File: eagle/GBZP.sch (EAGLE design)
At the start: 35 parts, among them CN1 USB-SMD-NS, J3 battery, X3 16MHz

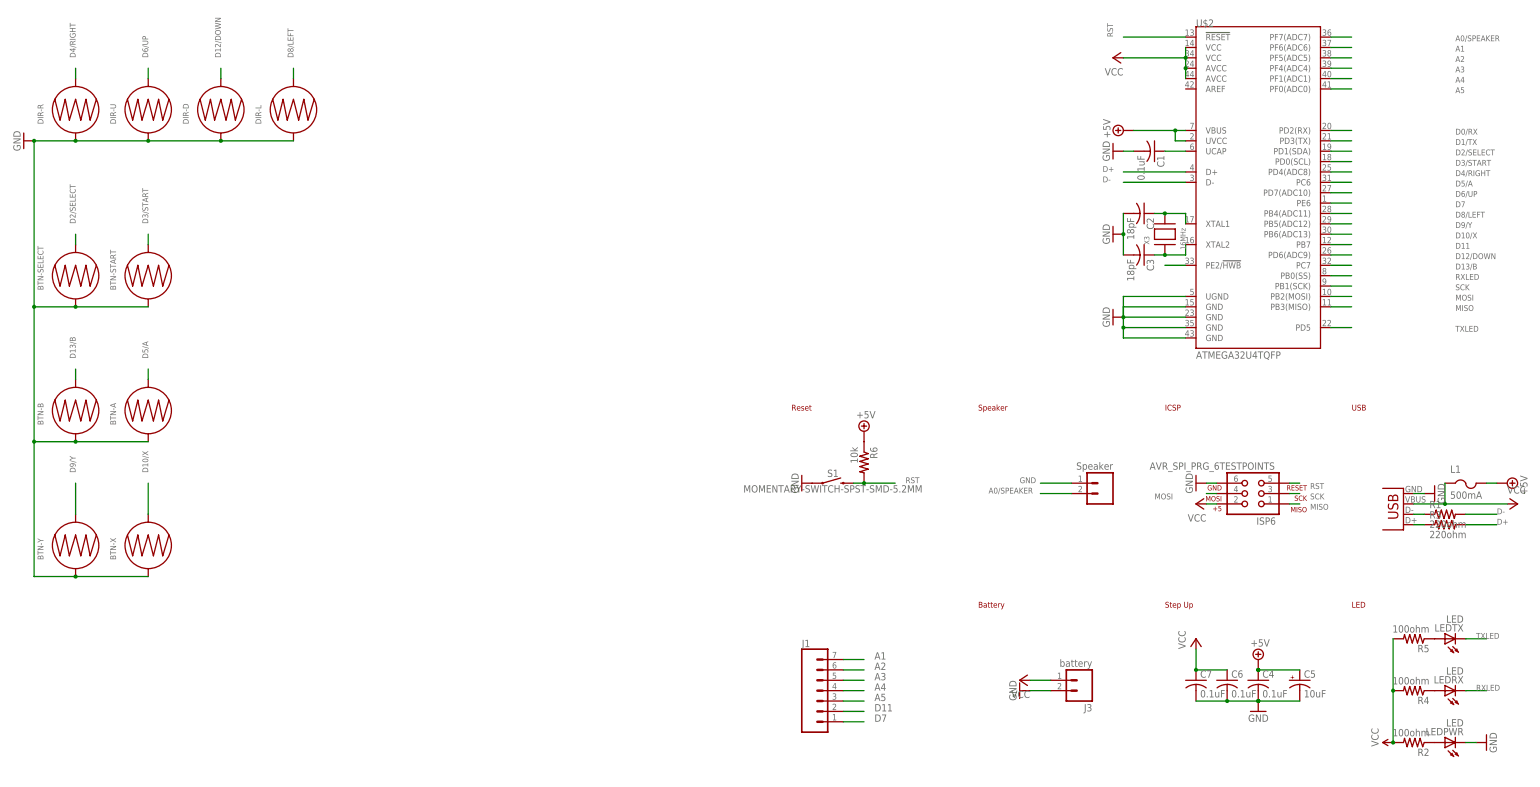
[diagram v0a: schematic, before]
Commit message: new pinout to match GBZ project
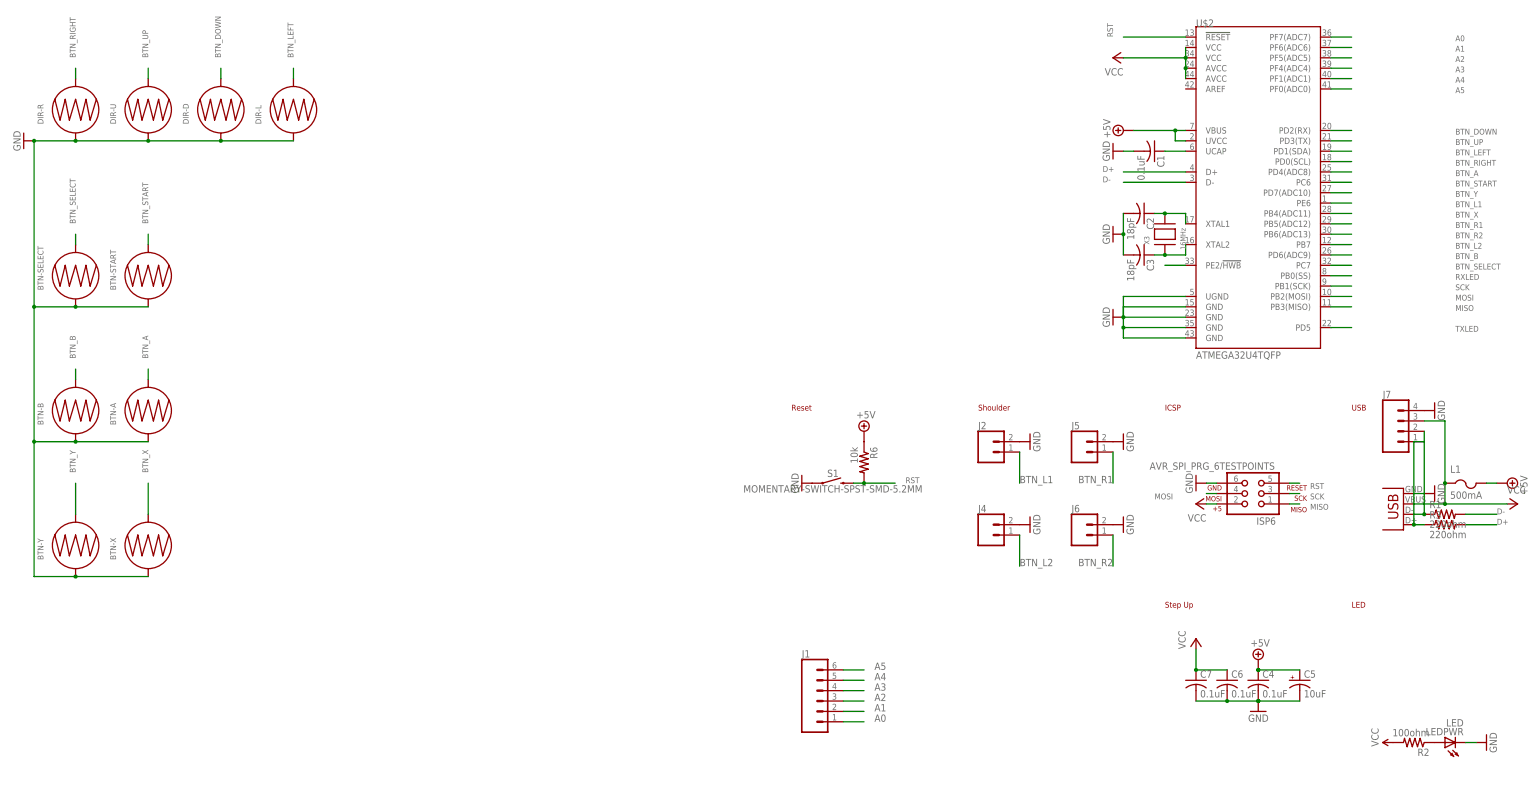
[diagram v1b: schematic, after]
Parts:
- removed J3: battery, SparkFun-Connectors:M021X02_NO_SILK
- removed JP2: Speaker, SparkFun-Connectors:M021X02_NO_SILK
- removed LEDRX, LEDTX: LED, adafruit:LEDCHIPLED_0805
- removed R4, R5: 100ohm, adafruit:R-US_R0805
- added J2, J4, J5, J6: (no value), SparkFun-Connectors:CONN_021X02_NO_SILK
- added J7: (no value), SparkFun-Connectors:CONN_041X04_NO_SILK
- J1: device SparkFun-Connectors:CONN_07NO_SILK -> SparkFun-Connectors:CONN_06NO_SILK_FEMALE_PTH
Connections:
- removed net A0/SPEAKER: JP2.2, U$2.PF7(ADC7)
- removed net D0/RX: U$2.PD2(RX)
- removed net D1/TX: U$2.PD3(TX)
- removed net D10/X: BTN-X.2, U$2.PB6(ADC13)
- removed net D11: J1.2, U$2.PB7
- removed net D12/DOWN: DIR-D.2, U$2.PD6(ADC9)
- removed net D13/B: BTN-B.2, U$2.PC7
- removed net D2/SELECT: BTN-SELECT.2, U$2.PD1(SDA)
- removed net D3/START: BTN-START.2, U$2.PD0(SCL)
- removed net D4/RIGHT: DIR-R.2, U$2.PD4(ADC8)
- removed net D5/A: BTN-A.2, U$2.PC6
- removed net D6/UP: DIR-U.2, U$2.PD7(ADC10)
- removed net D7: J1.1, U$2.PE6
- removed net D8/LEFT: DIR-L.2, U$2.PB4(ADC11)
- removed net D9/Y: BTN-Y.2, U$2.PB5(ADC12)
- removed net N$3: CN1.D+, R3.1
- removed net N$5: CN1.D-, R1.1
- removed net N$6: LEDRX.A, R4.1
- removed net N$7: LEDTX.A, R5.1
- new net A0: J1.1, U$2.PF7(ADC7)
- new net BTN_A: BTN-A.2, U$2.PD4(ADC8)
- new net BTN_B: BTN-B.2, U$2.PD6(ADC9)
- new net BTN_DOWN: DIR-D.2, U$2.PD2(RX)
- new net BTN_L1: J2.1, U$2.PE6
- new net BTN_L2: J4.1, U$2.PB7
- new net BTN_LEFT: DIR-L.2, U$2.PD1(SDA)
- new net BTN_R1: J5.1, U$2.PB5(ADC12)
- new net BTN_R2: J6.1, U$2.PB6(ADC13)
- new net BTN_RIGHT: DIR-R.2, U$2.PD0(SCL)
- new net BTN_SELECT: BTN-SELECT.2, U$2.PC7
- new net BTN_START: BTN-START.2, U$2.PC6
- new net BTN_UP: DIR-U.2, U$2.PD3(TX)
- new net BTN_X: BTN-X.2, U$2.PB4(ADC11)
- new net BTN_Y: BTN-Y.2, U$2.PD7(ADC10)
- new net D+IN: CN1.D+, J7.1, R3.1
- new net D-IN: CN1.D-, J7.2, R1.1
- net A1: now also J1.2; no longer J1.7
- net A2: now also J1.3; no longer J1.6
- net A3: now also J1.4; no longer J1.5
- net A4: now also J1.5; no longer J1.4
- net A5: now also J1.6; no longer J1.3
- net GND: now also J2.2, J4.2, J5.2, J6.2, J7.4; no longer J3.2, JP2.1
- net RXLED: no longer LEDRX.C
- net TXLED: no longer LEDTX.C
- net VCC: now also J7.3; no longer J3.1, R4.2, R5.2
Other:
- note added: "Shoulder"
- note removed: "Battery"
- note removed: "Speaker"

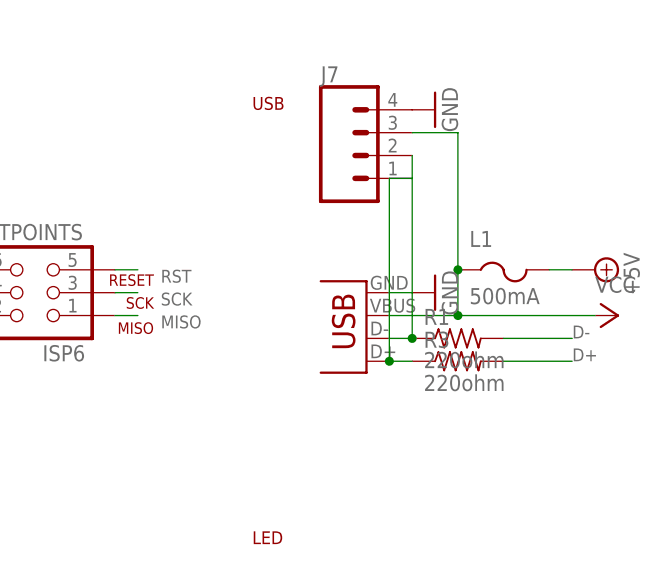
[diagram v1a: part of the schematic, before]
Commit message: Mon Apr  3 10:04:51 EDT 2017 - added new pin mapping
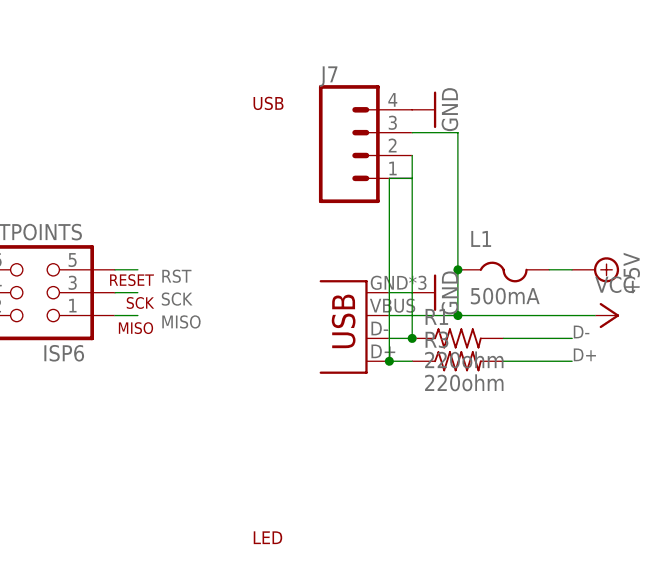
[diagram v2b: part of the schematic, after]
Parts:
- CN1: value USB-SMD-NS -> USB-MICROB; device SparkFun-Connectors:USB-SMD-NS -> SparkFun-Connectors:USB-MICROB
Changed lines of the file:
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@@
 <grid distance="0.1" unitdist="inch" unit="inch" style="lines" multiple="1" display="no" altdistance="0.01" altunitdist="inch" altunit="inch"/>
 <layers>
-<layer number="1" name="Top" color="4" fill="1" visible="no" active="no"/>
-<layer number="2" name="Route2" color="1" fill="3" visible="no" active="no"/>
-<layer number="3" name="Route3" color="4" fill="3" visible="no" active="no"/>
-<layer number="4" name="Route4" color="1" fill="4" visible="no" active="no"/>
-<layer number="5" name="Route5" color="4" fill="4" visible="no" active="no"/>
-<layer number="6" name="Route6" color="1" fill="8" visible="no" active="no"/>
-<layer number="7" name="Route7" color="4" fill="8" visible="no" active="no"/>
-<layer number="8" name="Route8" color="1" fill="2" visible="no" active="no"/>
-<layer number="9" name="Route9" color="4" fill="2" visible="no" active="no"/>
-<layer number="10" name="Route10" color="1" fill="7" visible="no" active="no"/>
-<layer number="11" name="Route11" color="4" fill="7" visible="no" active="no"/>
-<layer number="12" name="Route12" color="1" fill="5" visible="no" active="no"/>
-<layer number="13" name="Route13" color="4" fill="5" visible="no" active="no"/>
-<layer number="14" name="Route14" color="1" fill="6" visible="no" active="no"/>
-<layer number="15" name="Route15" color="4" fill="6" visible="no" active="no"/>
-<layer number="16" name="Bottom" color="1" fill="1" visible="no" active="no"/>
-<layer number="17" name="Pads" color="2" fill="1" visible="no" active="no"/>
-<layer number="18" name="Vias" color="2" fill="1" visible="no" active="no"/>
-<layer number="19" name="Unrouted" color="6" fill="1" visible="no" active="no"/>
-<layer number="20" name="Dimension" color="15" fill="1" visible="no" active="no"/>
-<layer number="21" name="tPlace" color="7" fill="1" visible="no" active="no"/>
-<layer number="22" name="bPlace" color="7" fill="1" visible="no" active="no"/>
-<layer number="23" name="tOrigins" color="15" fill="1" visible="no" active="no"/>
-<layer number="24" name="bOrigins" color="15" fill="1" visible="no" active="no"/>
-<layer number="25" name="tNames" color="7" fill="1" visible="no" active="no"/>
-<layer number="26" name="bNames" color="7" fill="1" visible="no" active="no"/>
-<layer number="27" name="tValues" color="7" fill="1" visible="no" active="no"/>
-<layer number="28" name="bValues" color="7" fill="1" visible="no" active="no"/>
+<layer number="1" name="Top" color="4" fill="1" visible="yes" active="no"/>
+<layer number="2" name="Route2" color="1" fill="3" visible="yes" active="no"/>
+<layer number="3" name="Route3" color="4" fill="3" visible="yes" active="no"/>
+<layer number="4" name="Route4" color="1" fill="4" visible="yes" active="no"/>
+<layer number="5" name="Route5" color="4" fill="4" visible="yes" active="no"/>
+<layer number="6" name="Route6" color="1" fill="8" visible="yes" active="no"/>
+<layer number="7" name="Route7" color="4" fill="8" visible="yes" active="no"/>
+<layer number="8" name="Route8" color="1" fill="2" visible="yes" active="no"/>
+<layer number="9" name="Route9" color="4" fill="2" visible="yes" active="no"/>
+<layer number="10" name="Route10" color="1" fill="7" visible="yes" active="no"/>
+<layer number="11" name="Route11" color="4" fill="7" visible="yes" active="no"/>
+<layer number="12" name="Route12" color="1" fill="5" visible="yes" active="no"/>
+<layer number="13" name="Route13" color="4" fill="5" visible="yes" active="no"/>
+<layer number="14" name="Route14" color="1" fill="6" visible="yes" active="no"/>
+<layer number="15" name="Route15" color="4" fill="6" visible="yes" active="no"/>
+<layer number="16" name="Bottom" color="1" fill="1" visible="yes" active="no"/>
+<layer number="17" name="Pads" color="2" fill="1" visible="yes" active="no"/>
+<layer number="18" name="Vias" color="2" fill="1" visible="yes" active="no"/>
+<layer number="19" name="Unrouted" color="6" fill="1" visible="yes" active="no"/>
+<layer number="20" name="Dimension" color="15" fill="1" visible="yes" active="no"/>
+<layer number="21" name="tPlace" color="7" fill="1" visible="yes" active="no"/>
+<layer number="22" name="bPlace" color="7" fill="1" visible="yes" active="no"/>
+<layer number="23" name="tOrigins" color="15" fill="1" visible="yes" active="no"/>
+<layer number="24" name="bOrigins" color="15" fill="1" visible="yes" active="no"/>
+<layer number="25" name="tNames" color="7" fill="1" visible="yes" active="no"/>
+<layer number="26" name="bNames" color="7" fill="1" visible="yes" active="no"/>
+<layer number="27" name="tValues" color="7" fill="1" visible="yes" active="no"/>
+<layer number="28" name="bValues" color="7" fill="1" visible="yes" active="no"/>
 <layer number="29" name="tStop" color="7" fill="3" visible="no" active="no"/>
 <layer number="30" name="bStop" color="7" fill="6" visible="no" active="no"/>
@@
 <layer number="35" name="tGlue" color="7" fill="4" visible="no" active="no"/>
 <layer number="36" name="bGlue" color="7" fill="5" visible="no" active="no"/>
-<layer number="37" name="tTest" color="7" fill="1" visible="no" active="no"/>
-<layer number="38" name="bTest" color="7" fill="1" visible="no" active="no"/>
+<layer number="37" name="tTest" color="7" fill="1" visible="yes" active="no"/>
+<layer number="38" name="bTest" color="7" fill="1" visible="yes" active="no"/>
 <layer number="39" name="tKeepout" color="4" fill="11" visible="no" active="no"/>
 <layer number="40" name="bKeepout" color="1" fill="11" visible="no" active="no"/>
@@
 <layer number="44" name="Drills" color="7" fill="1" visible="no" active="no"/>
 <layer number="45" name="Holes" color="7" fill="1" visible="no" active="no"/>
-<layer number="46" name="Milling" color="3" fill="1" visible="no" active="no"/>
-<layer number="47" name="Measures" color="7" fill="1" visible="no" active="no"/>
-<layer number="48" name="Document" color="7" fill="1" visible="no" active="no"/>
-<layer number="49" name="Reference" color="7" fill="1" visible="no" active="no"/>
-<layer number="50" name="dxf" color="7" fill="1" visible="no" active="no"/>
-<layer number="51" name="tDocu" color="7" fill="1" visible="no" active="no"/>
-<layer number="52" name="bDocu" color="7" fill="1" visible="no" active="no"/>
-<layer number="53" name="tGND_GNDA" color="7" fill="9" visible="no" active="no"/>
-<layer number="54" name="bGND_GNDA" color="1" fill="9" visible="no" active="no"/>
-<layer number="56" name="wert" color="7" fill="1" visible="no" active="no"/>
-<layer number="57" name="tCAD" color="7" fill="1" visible="no" active="no"/>
-<layer number="59" name="tCarbon" color="7" fill="1" visible="no" active="no"/>
-<layer number="60" name="bCarbon" color="7" fill="1" visible="no" active="no"/>
+<layer number="46" name="Milling" color="3" fill="1" visible="yes" active="no"/>
+<layer number="47" name="Measures" color="7" fill="1" visible="yes" active="no"/>
+<layer number="48" name="Document" color="7" fill="1" visible="yes" active="no"/>
+<layer number="49" name="Reference" color="7" fill="1" visible="yes" active="no"/>
+<layer number="50" name="dxf" color="7" fill="1" visible="yes" active="no"/>
+<layer number="51" name="tDocu" color="7" fill="1" visible="yes" active="no"/>
+<layer number="52" name="bDocu" color="7" fill="1" visible="yes" active="no"/>
+<layer number="53" name="tGND_GNDA" color="7" fill="9" visible="yes" active="no"/>
+<layer number="54" name="bGND_GNDA" color="1" fill="9" visible="yes" active="no"/>
+<layer number="56" name="wert" color="7" fill="1" visible="yes" active="no"/>
+<layer number="57" name="tCAD" color="7" fill="1" visible="yes" active="no"/>
+<layer number="59" name="tCarbon" color="7" fill="1" visible="yes" active="no"/>
+<layer number="60" name="bCarbon" color="7" fill="1" visible="yes" active="no"/>
 <layer number="90" name="Modules" color="5" fill="1" visible="yes" active="yes"/>
 <layer number="91" name="Nets" color="2" fill="1" visible="yes" active="yes"/>
@@
 <part name="C6" library="adafruit" deviceset="C-US" device="C0805" value="0.1uF"/>
 <part name="C7" library="adafruit" deviceset="C-US" device="C0805" value="0.1uF"/>
-<part name="CN1" library="SparkFun-Connectors" deviceset="USB" device="-SMD-NS" value="USB-SMD-NS"/>
+<part name="CN1" library="SparkFun-Connectors" deviceset="USB" device="-MICROB" value="USB-MICROB"/>
 <part name="P+1" library="supply1" deviceset="VCC" device=""/>
 <part name="P+3" library="supply1" deviceset="VCC" device=""/>

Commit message: Wed Aug  9 10:25:52 EDT 2017 new version of GBZP
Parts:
- removed R6: 10k, adafruit:R-US_R0805
- removed S1: MOMENTARY-SWITCH-SPST-SMD-5.2MM, SparkFun-Switches:MOMENTARY-SWITCH-SPST-SMD-5.2MM
- BTN-A, BTN-B, BTN-SELECT, BTN-START, BTN-X, BTN-Y, DIR-D, DIR-L, DIR-R, DIR-U: value BUTTON-CONDUCTIVESMD -> (none); device SparkFun-Electromechanical:BUTTON-CONDUCTIVESMD -> switch-padswitch:PADSWITCH
- C1, C2, C3, C4, C6, C7: device adafruit:C-USC0805 -> adafruit:C-USC0402K
- LEDPWR: device adafruit:LEDCHIPLED_0805 -> adafruit:LEDCHIP-LED0603
- R1, R2, R3: device adafruit:R-US_R0805 -> adafruit:R-US_R0402
- X3: device adaprog:XTALNX5032 -> adafruit:XTAL-3.2X1.5
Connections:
- net +5V: no longer R6.1
- net GND: no longer S1.1
- net RST: no longer R6.2, S1.2

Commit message: Fri Sep 29 08:38:18 EDT 2017 - cleaning schematics
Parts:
- removed BTN-A, BTN-B, BTN-SELECT, BTN-START, BTN-X, BTN-Y, DIR-D, DIR-L, DIR-R, DIR-U: (no value), switch-padswitch:PADSWITCH
- removed C1, C4, C6, C7: 0.1uF, adafruit:C-USC0402K
- removed C2, C3: 18pF, adafruit:C-USC0402K
- removed C5: 10uF, SparkFun-Retired:10UF-TANT
- removed CN1: USB-MICROB, SparkFun-Connectors:USB-MICROB
- removed ISP6: AVR_SPI_PRG_6TESTPOINTS, SparkFun-Connectors:AVR_SPI_PRG_6TESTPOINTS
- removed J1: (no value), SparkFun-Connectors:CONN_06NO_SILK_FEMALE_PTH
- removed J2, J4, J5, J6: (no value), SparkFun-Connectors:CONN_021X02_NO_SILK
- removed J7: (no value), SparkFun-Connectors:CONN_041X04_NO_SILK
- removed L1: 500mA, adafruit:PTCFUSE-1206
- removed LEDPWR: LED, adafruit:LEDCHIP-LED0603
- removed R1, R3: 220ohm, adafruit:R-US_R0402
- removed R2: 100ohm, adafruit:R-US_R0402
- removed U$2: ATMEGA32U4TQFP, SparkFun-Retired:ATMEGA32U4TQFP
- removed X3: 16MHz, adafruit:XTAL-3.2X1.5
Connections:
- removed net +5V: C4.1, C5.+, L1.2, U$2.UVCC, U$2.VBUS
- removed net A0: J1.1, U$2.PF7(ADC7)
- removed net A1: J1.2, U$2.PF6(ADC6)
- removed net A2: J1.3, U$2.PF5(ADC5)
- removed net A3: J1.4, U$2.PF4(ADC4)
- removed net A4: J1.5, U$2.PF1(ADC1)
- removed net A5: J1.6, U$2.PF0(ADC0)
- removed net BTN_A: BTN-A.2, U$2.PD4(ADC8)
- removed net BTN_B: BTN-B.2, U$2.PD6(ADC9)
- removed net BTN_DOWN: DIR-D.2, U$2.PD2(RX)
- removed net BTN_L1: J2.1, U$2.PE6
- removed net BTN_L2: J4.1, U$2.PB7
- removed net BTN_LEFT: DIR-L.2, U$2.PD1(SDA)
- removed net BTN_R1: J5.1, U$2.PB5(ADC12)
- removed net BTN_R2: J6.1, U$2.PB6(ADC13)
- removed net BTN_RIGHT: DIR-R.2, U$2.PD0(SCL)
- removed net BTN_SELECT: BTN-SELECT.2, U$2.PC7
- removed net BTN_START: BTN-START.2, U$2.PC6
- removed net BTN_UP: DIR-U.2, U$2.PD3(TX)
- removed net BTN_X: BTN-X.2, U$2.PB4(ADC11)
- removed net BTN_Y: BTN-Y.2, U$2.PD7(ADC10)
- removed net D+: R3.2, U$2.D+
- removed net D+IN: CN1.D+, J7.1, R3.1
- removed net D-: R1.2, U$2.D-
- removed net D-IN: CN1.D-, J7.2, R1.1
- removed net GND: BTN-A.1, BTN-B.1, BTN-SELECT.1, BTN-START.1, BTN-X.1, BTN-Y.1, C1.2, C2.2, C3.2, C4.2, C5.-, C6.2, C7.2, CN1.GND, DIR-D.1, DIR-L.1, DIR-R.1, DIR-U.1, ISP6.6, J2.2, J4.2, J5.2, J6.2, J7.4, LEDPWR.C, U$2.GND@15, U$2.GND@23, U$2.GND@35, U$2.GND@43, U$2.UGND
- removed net HWB: U$2.PE2/!HWB
- removed net MISO: ISP6.1, U$2.PB3(MISO)
- removed net MOSI: ISP6.4, U$2.PB2(MOSI)
- removed net N$2: LEDPWR.A, R2.1
- removed net N$8: C2.1, U$2.XTAL1, X3.P$2
- removed net N$9: C3.1, U$2.XTAL2, X3.P$1
- removed net RST: ISP6.5, U$2.!RESET
- removed net RXLED: U$2.PB0(SS)
- removed net SCK: ISP6.3, U$2.PB1(SCK)
- removed net TXLED: U$2.PD5
- removed net UCAP: C1.1, U$2.UCAP
- removed net VCC: C6.1, C7.1, CN1.VBUS, ISP6.2, J7.3, L1.1, R2.2, U$2.AVCC@24, U$2.AVCC@44, U$2.VCC@14, U$2.VCC@34
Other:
- note removed: "ICSP"
- note removed: "LED"
- note removed: "Reset"
- note removed: "Shoulder"
- note removed: "Step Up"
- note removed: "USB"
